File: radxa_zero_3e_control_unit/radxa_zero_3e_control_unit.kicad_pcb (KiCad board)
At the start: 2 copper layers, 186 x 65 mm, 122 parts, among them J1 USB STM32, J10 Valve, J11 ETH_IN, J12 ETH_OUT, J13 Compressor, J14 DebugUART, J15 Weight, J16 Malibotti, J17 Robot, J18 STLINK_V3_MINIE, J19 IO, J2 DC IN, J20 Bus-Servo, J21 STDC14, J22 USB STM32, J23 IO, J24 IO, J3 TOF3, J4 TOF2, J5 TOF1, J6 TOF1, J7 STEP1, J8 STEP2, J9 Conveyor, Q1 BC807, Q2 IRLML6344, Q3 IRLML6344, Q4 IRLML6344, U1 TPS54202DDC, U2 STM32G431RBTx, U3 HX711, U4 DCDC_MP2315, U5 TMC2209, U6 TMC2209, U7 PoE->24V, X1 Radxa Zero 3E

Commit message: Various
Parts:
- added J25: IO, Connector_JST:JST_XH_B6B-XH-A_1x06_P2.50mm_Vertical, F.Cu at (116.2, 95.7)
- added J26: IO, Connector_JST:JST_XH_B6B-XH-A_1x06_P2.50mm_Vertical, F.Cu at (156.6, 64.0)
- added J27: IO, Connector_JST:JST_XH_B6B-XH-A_1x06_P2.50mm_Vertical, F.Cu at (60.2, 93.4)
- C23: footprint Capacitor_THT:CP_Radial_D6.3mm_P2.50mm -> Capacitor_THT:CP_Radial_D8.0mm_P2.50mm
- moved FID2 8.33 mm to (152.7, 72.2)
- moved C23 0.90 mm to (150.1, 68.0)
- moved C33 0.50 mm to (122.2, 68.7)
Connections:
- J2 pad 1: GND -> 5-24V
- J2 pad 2: 5-24V -> GND
- J2 pad 3: unconnected-(J2-Pad3) -> GND
- U5 pad 9: GND -> +3V3
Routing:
- net +5V: track 96.6 -> 104.7 mm
- net +3V3: track 295.6 -> 302.3 mm, vias 9 -> 10
- net USBPD_D-: track 37.6 -> 42.5 mm
- net USBPD_D+: track 38.6 -> 42.9 mm
- net USB_VSENSE: track 49.4 -> 51.9 mm
- net 5-24V: track 177.1 -> 179.0 mm
- net GND: track 89.6 -> 91.6 mm, vias 347 -> 361
- net i2d: track 37.0 -> 37.7 mm
- net i2c: track 39.1 -> 39.8 mm
- net i1c: track 81.7 -> 82.4 mm
- net +9V: track 42.3 -> 43.0 mm
- net INT_TOF2: track 25.6 -> 26.3 mm
- net INT_TOF1: track 75.0 -> 75.7 mm
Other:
- board text added: "24V"
- board text added: "Stepper0"
- board text removed: "Stepper2"

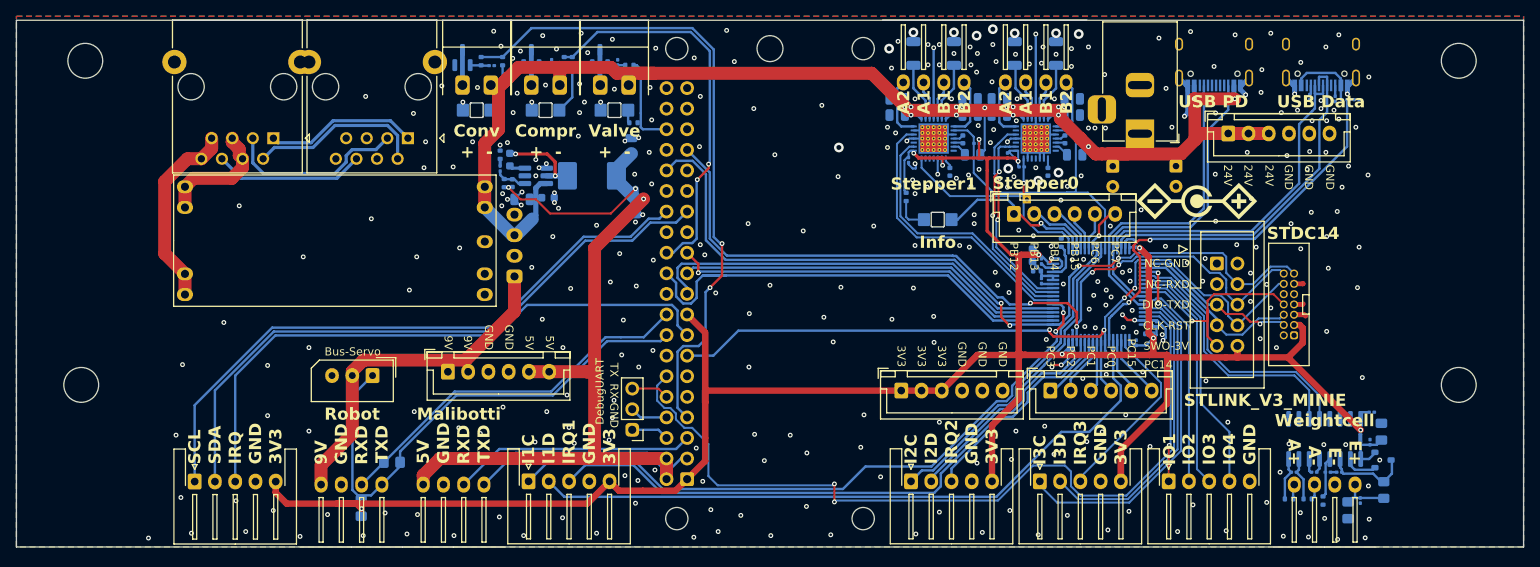
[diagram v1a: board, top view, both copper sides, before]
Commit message: Fixes
- air ventilation holes
- HX711 is on SPI MISO and SPI MOSI according to https://github.com/ufnalski/hx711_non_blocking_spi_g431kb (PC10-->PC11, PC11-->PC12)
- DC connector polarity changed
- connectors for voltages
- TMC2209 got different communication IDs
- Elkos mor space
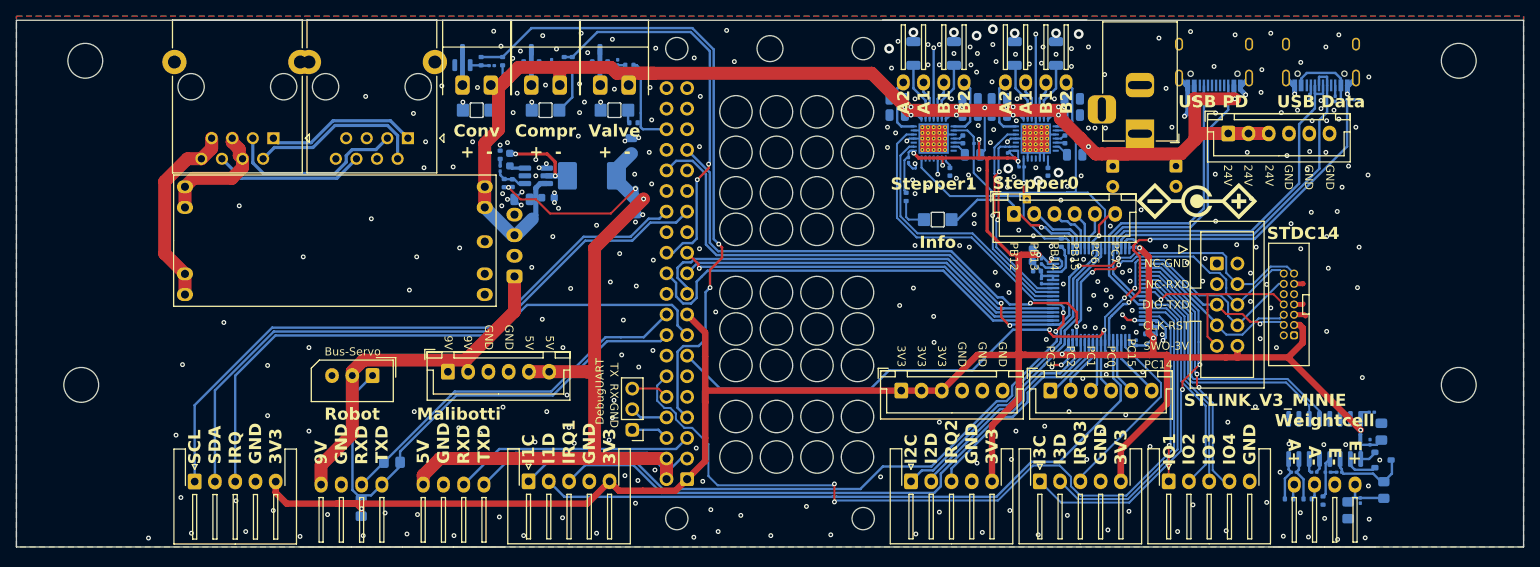
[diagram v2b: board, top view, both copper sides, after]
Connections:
- U2 pad 52: HX711_DATA -> IO4
- U2 pad 53: HX711_CLK -> HX711_DATA
- U2 pad 54: IO4 -> HX711_CLK
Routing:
- net STM32_RESET: track 91.2 -> 94.6 mm
- net SPI1_NSS: track 57.9 -> 55.6 mm
- net i3c: track 46.5 -> 48.1 mm
- net IO2: track 26.1 -> 27.6 mm
- net SWO: track 27.2 -> 26.2 mm
- net IO4: track 30.3 -> 31.1 mm, vias 0 -> 2
- net STEPPER_UART: track 31.5 -> 30.7 mm
- net HX711_DATA: track 33.1 -> 33.8 mm
- net HX711_CLK: track 32.0 -> 32.7 mm
- net IO3: track 28.7 -> 27.9 mm
- net SPI1_MISO: track 47.7 -> 48.2 mm
- net GND: vias 361 -> 340
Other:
- outline, holes or cut-outs redrawn

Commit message: WIP, before repinning SUM32G431
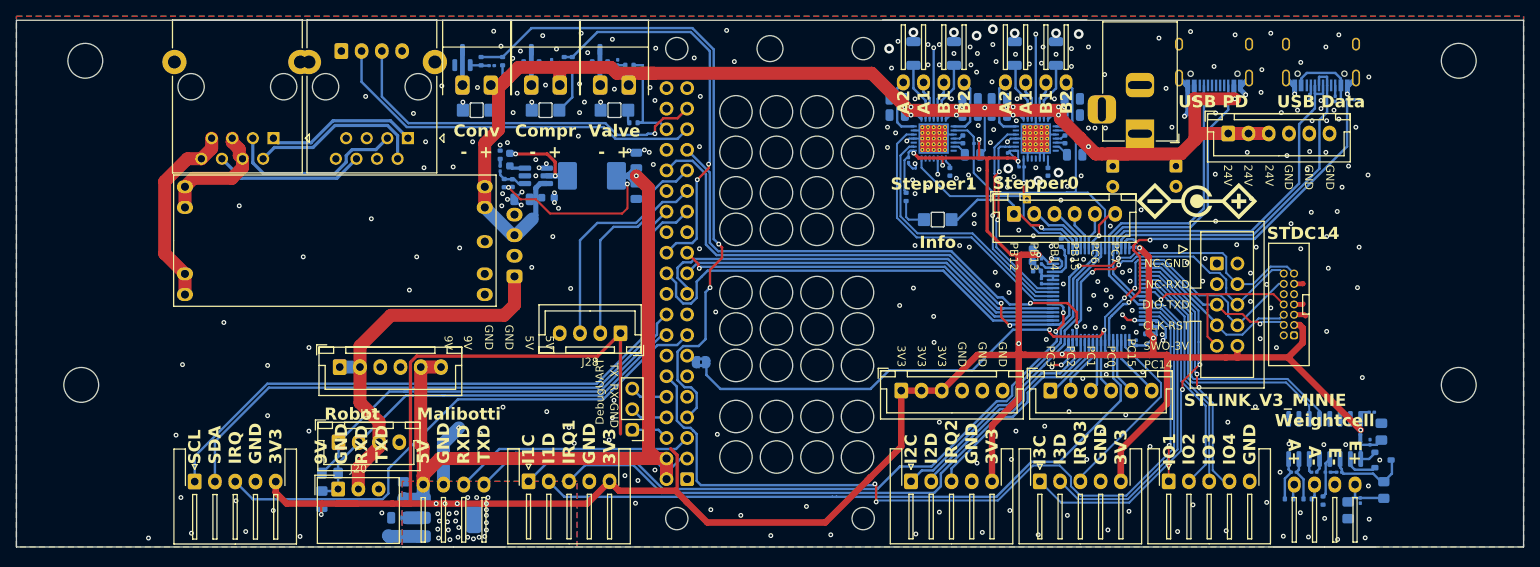
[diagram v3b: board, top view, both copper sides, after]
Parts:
- added C31: 10u, Capacitor_SMD:C_0805_2012Metric_Pad1.18x1.45mm_HandSolder, B.Cu at (54.8, 108.0)
- added C32: 22u, Capacitor_SMD:C_0805_2012Metric, B.Cu at (54.2, 111.4)
- added J28: RADXA I2C, Connector_JST:JST_XH_B4B-XH-A_1x04_P2.50mm_Vertical, F.Cu at (81.5, 88.6)
- added J29: RADXA GPIO, Connector_JST:JST_XH_B4B-XH-A_1x04_P2.50mm_Vertical, B.Cu at (47.1, 53.8)
- added JP1: STM_RST, Jumper:SolderJumper-2_P1.3mm_Bridged2Bar_RoundedPad1.0x1.5mm, B.Cu at (91.5, 92.2)
- added R33: 1k, Resistor_SMD:R_0402_1005Metric, B.Cu at (130.7, 88.9)
- added U8: AMS1117-3.3, Package_TO_SOT_SMD:SOT-223-3_TabPin2, B.Cu at (60.3, 111.4)
- J17: footprint liebler_CONN:JST_XH_S4B-XH-A-1_1x04_P2.50mm_Horizontal_SmallerCourtyard -> Connector_JST:JST_XH_B4B-XH-A_1x04_P2.50mm_Vertical
- J20: footprint Connector_Molex:Molex_SPOX_5267-03A_1x03_P2.50mm_Vertical -> Connector_Molex:Molex_SPOX_5268-03A_1x03_P2.50mm_Horizontal
- moved J20 14.6 mm to (46.7, 107.9), turned to 0 degrees
- moved J27 13.4 mm to (46.9, 92.8)
- moved R77 7.77 mm to (45.7, 105.9)
- moved J17 5.65 mm to (46.8, 102.1)
- moved R76 4.97 mm to (44.7, 109.1)
- moved C5 1.90 mm to (83.5, 71.1)
- moved C7 1.90 mm to (83.5, 67.3)
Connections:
- J17 pad 1: +9V -> ROBOT_RXD
- J17 pad 2: GND -> ROBOT_TXD
- J17 pad 3: ROBOT_RXD -> +9V
- J17 pad 4: ROBOT_TXD -> GND
- X1 pad 1: +3V3 -> unconnected-(X1-3V3-Pad1)
- X1 pad 13: STM32_RESET -> Net-(JP1-B)
- X1 pad 17: +3V3 -> unconnected-(X1-3V3-Pad17)
- X1 pad 29: unconnected-(X1-G3B3/-/-/I5C_SCL-Pad29) -> I5C_C
- X1 pad 31: unconnected-(X1-G3B4/-/-/I5C_SSDA-Pad31) -> I5C_D
- X1 pad 35: unconnected-(X1-G3A4/-/I3S_LRCK-Pad35) -> G3A4
- X1 pad 37: unconnected-(X1-G1A4/-/I1S_SCLK-Pad37) -> G1A4
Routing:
- net +3V3: track 302.3 -> 361.0 mm, vias 10 -> 38
- net G3A4: track 0.00 -> 47.4 mm
- net G1A4: track 0.00 -> 47.1 mm, vias 0 -> 1
- net I5C_D: track 0.00 -> 29.4 mm
- net I5C_C: track 0.00 -> 24.7 mm
- net +5V: track 104.7 -> 119.4 mm
- net GND: track 91.6 -> 103.6 mm, vias 340 -> 310
- net ROBOT_TXD: track 63.4 -> 52.6 mm
- net INT_RGB: track 75.1 -> 66.8 mm
- net ROBOT_RXD: track 46.3 -> 53.4 mm
- net +9V: track 43.0 -> 46.9 mm
- net SCL: track 77.6 -> 81.3 mm
- net SDA: track 78.7 -> 82.3 mm
- net STM32_RESET: track 94.6 -> 92.8 mm
- net Conveyor_PWM: track 81.0 -> 82.4 mm
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- added copper zone on B.Cu, net +3V3
- added copper zone on F.Cu, net +3V3
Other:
- board text added: "- +"
- board text removed: "+ -"

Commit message: Udated control unit pcb
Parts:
- removed J11: ETH_IN, liebler_CONN:RJ45_WithoutMagneticsTHT
- removed J17: Robot, Connector_JST:JST_XH_B4B-XH-A_1x04_P2.50mm_Vertical
- removed J18: STLINK_V3_MINIE, Connector_IDC:IDC-Header_2x05_P2.54mm_Vertical
- removed J19: IO, Connector_JST:JST_XH_S5B-XH-A-1_1x05_P2.50mm_Horizontal
- removed J23, J24, J25, J26, J27: IO, Connector_JST:JST_XH_B6B-XH-A_1x06_P2.50mm_Vertical
- removed J28: RADXA I2C, Connector_JST:JST_XH_B4B-XH-A_1x04_P2.50mm_Vertical
- removed J29: RADXA GPIO, Connector_JST:JST_XH_B4B-XH-A_1x04_P2.50mm_Vertical
- added C41: u1, Capacitor_SMD:C_0402_1005Metric, B.Cu at (48.2, 75.5)
- added H3: M2,5, MountingHole:MountingHole_2.7mm, F.Cu at (137.5, 53.5)
- added H4: M2,5, MountingHole:MountingHole_2.7mm, F.Cu at (137.5, 111.5)
- added J30: LightBarrier1, liebler_CONN:JST_XH_B3B-XH-A_1x03_P2.50mm_Vertical_smaller, F.Cu at (67.1, 66.4)
- added J31: LightBarrier2, liebler_CONN:JST_XH_B3B-XH-A_1x03_P2.50mm_Vertical_smaller, F.Cu at (67.1, 60.2)
- added J32: LightBarrier3, liebler_CONN:JST_XH_B3B-XH-A_1x03_P2.50mm_Vertical_smaller, F.Cu at (56.8, 60.2)
- added J33: PressureTransducer, liebler_CONN:JST_XH_B3B-XH-A_1x03_P2.50mm_Vertical_smaller, F.Cu at (79.8, 53.8)
- added JP2: 5-24, Jumper:SolderJumper-3_P1.3mm_Open_RoundedPad1.0x1.5mm_NumberLabels, B.Cu at (67.1, 64.6)
- added JP3: 5-24, Jumper:SolderJumper-3_P1.3mm_Open_RoundedPad1.0x1.5mm_NumberLabels, B.Cu at (67.1, 58.4)
- added JP4: 5-24, Jumper:SolderJumper-3_P1.3mm_Open_RoundedPad1.0x1.5mm_NumberLabels, B.Cu at (56.8, 58.4)
- added M1: W5500_mini, liebler_MODULES:W5500-mini, F.Cu at (98.2, 82.5)
- added M2: FanMech, liebler_MECH:FAN2507, F.Cu at (113.0, 82.5)
- added M3: FanElek, Connector_JST:JST_XH_B2B-XH-A_1x02_P2.50mm_Vertical, F.Cu at (79.8, 66.4)
- added R32: 10k, Resistor_SMD:R_0402_1005Metric, B.Cu at (83.4, 56.0)
- added R34: 10k, Resistor_SMD:R_0402_1005Metric, B.Cu at (82.9, 63.4)
- added R35: 10k, Resistor_SMD:R_0402_1005Metric, B.Cu at (53.4, 71.8)
- added R36: 1k, Resistor_SMD:R_0402_1005Metric, B.Cu at (50.0, 79.2)
- added X2: MT3608, liebler_MODULES:DCDC_MT3608, B.Cu at (136.2, 82.8)
- C11, C12, C13, C15, C16, C17, C18, C19, C20, C21, C27, C28, C6, C9: footprint Capacitor_SMD:C_0201_0603Metric -> Capacitor_SMD:C_0402_1005Metric
- C24: footprint Capacitor_THT:CP_Radial_D6.3mm_P2.50mm -> Capacitor_THT:CP_Radial_D8.0mm_P2.50mm
- C31: footprint Capacitor_SMD:C_0805_2012Metric_Pad1.18x1.45mm_HandSolder -> Capacitor_SMD:C_0805_2012Metric
- H6: footprint MountingHole:MountingHole_3.2mm_M3 -> MountingHole:MountingHole_2.7mm
- J12: value ETH_OUT -> CAN; footprint liebler_CONN:RJ45_WithoutMagneticsTHT -> liebler_CONN:JST_XH_B3B-XH-A_1x03_P2.50mm_Vertical_smaller
- J15, J16, J7, J8: footprint liebler_CONN:JST_XH_S4B-XH-A-1_1x04_P2.50mm_Horizontal_SmallerCourtyard -> liebler_CONN:JST_XH_B4B-XH-A_1x04_P2.50mm_Vertical_smaller
- J20: footprint Connector_Molex:Molex_SPOX_5268-03A_1x03_P2.50mm_Horizontal -> Connector_Molex:Molex_SPOX_5267-03A_1x03_P2.50mm_Vertical
- J3, J4, J5: footprint Connector_JST:JST_XH_S5B-XH-A-1_1x05_P2.50mm_Horizontal -> liebler_CONN:JST_XH_B5B-XH-A_1x05_P2.50mm_Vertical_smaller
- J6: value TOF1 -> RGB; footprint Connector_JST:JST_XH_S5B-XH-A-1_1x05_P2.50mm_Horizontal -> liebler_CONN:JST_XH_B5B-XH-A_1x05_P2.50mm_Vertical_smaller
- R10, R11, R21, R24, R27, R3, R8, R9: footprint Resistor_SMD:R_0201_0603Metric -> Resistor_SMD:R_0402_1005Metric
- R76, R77: footprint Resistor_SMD:R_0805_2012Metric_Pad1.20x1.40mm_HandSolder -> Resistor_SMD:R_0402_1005Metric
- TP1: footprint TestPoint:TestPoint_THTPad_1.0x1.0mm_Drill0.5mm -> TestPoint:TestPoint_THTPad_D1.0mm_Drill0.5mm
- U4: moved to B.Cu
- U7: value PoE->24V -> SIT3051TK; footprint liebler_MODULES:XC7010_DCDC_ISOLATED_MODUEL -> Package_DFN_QFN:DFN-8-1EP_3x3mm_P0.65mm_EP1.55x2.4mm; moved to B.Cu
- moved L2 159.1 mm to (26.0, 54.2), turned to -90 degrees
- moved Q1 157.9 mm to (24.7, 57.9), turned to 90 degrees
- moved C22 155.0 mm to (25.3, 62.4), turned to -90 degrees
- moved C20 154.6 mm to (25.3, 60.0), turned to 0 degrees
- moved C10 154.1 mm to (28.9, 51.8), turned to 180 degrees
- moved C6 152.5 mm to (31.8, 51.3), turned to 0 degrees
- moved R30 152.3 mm to (27.1, 105.6), turned to 90 degrees
- moved NT1 150.4 mm to (27.2, 63.9), turned to 180 degrees
- moved R29 150.2 mm to (27.9, 105.6), turned to -90 degrees
- moved R8 149.6 mm to (29.3, 55.6), turned to 0 degrees
- moved C21 149.4 mm to (28.9, 64.0)
- moved J22 149.0 mm to (30.4, 111.1), turned to 180 degrees
- moved R28 148.4 mm to (28.6, 105.6), turned to 90 degrees
- moved R7 147.9 mm to (31.8, 52.3), turned to 180 degrees
- moved R11 146.5 mm to (31.2, 55.6), turned to 0 degrees
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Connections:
- net PB12 renamed ADC1_IN11
- net i1c renamed I2C2_SCL
- net i1d renamed I2C2_SDA
- J10 pad 1: 5-24V -> +24V
- J12 pad 1: Net-(J11-Pad1) -> CANH
- J12 pad 2: Net-(J11-Pad2) -> GND
- J12 pad 3: Net-(J11-Pad3) -> CANL
- J13 pad 1: 5-24V -> +24V
- J16 pad 1: +5V -> MALIBOTTI_U1R
- J16 pad 2: GND -> MALIBOTTI_U1T
- J16 pad 3: MALIBOTTI_RXD -> GND
- J16 pad 4: MALIBOTTI_TXD -> +5V
- J20 pad 1: ROBOT_TXD -> ROBOT_U4R
- J3 pad 1: i3c -> I2C3_SCL
- J3 pad 2: i3d -> I2C3_SDA
- J4 pad 3: INT_TOF1 -> INT_TOF2
- J5 pad 1: i2c -> I2C1_SCL
- J5 pad 2: i2d -> I2C1_SDA
- J5 pad 3: INT_TOF2 -> INT_TOF1
- J6 pad 1: SCL -> I2C1_SCL
- J6 pad 2: SDA -> I2C1_SDA
- J9 pad 1: 5-24V -> +24V
- R19 pad 2: Conveyor_PWM -> CONVEYOR_T2C2
- R20 pad 2: Conveyor_PWM -> CONVEYOR_T2C2
- R22 pad 2: Valve -> VALVE
- R23 pad 2: Valve -> VALVE
- R25 pad 2: Compressor_PWM -> COMPRESSOR_T2C1
- R26 pad 2: Compressor_PWM -> COMPRESSOR_T2C1
- R76 pad 2: ROBOT_TXD -> ROBOT_U4R
- R77 pad 1: ROBOT_RXD -> ROBOT_U4T
- R77 pad 2: ROBOT_TXD -> ROBOT_U4R
- U2 pad 10: T1C3 -> PRESSURE_ADC
- U2 pad 11: T1C4 -> W5500_IRQ
- U2 pad 12: INT_TOF2 -> COMPRESSOR_T2C1
- U2 pad 13: INT_TOF1 -> CONVEYOR_T2C2
- U2 pad 2: INT_TOF3 -> LightBarrier3
- U2 pad 23: Stepper1_Dir -> VALVE
- U2 pad 24: Stepper1_Step -> STEPPER1_DIR
- U2 pad 25: Stepper2_Step -> STEPPER1_STEP
- U2 pad 26: Stepper2_Dir -> ADC2_12
- U2 pad 3: PC14 -> LightBarrier2
- U2 pad 35: PB13 -> STEPPER_EN
- U2 pad 36: T15C1 -> HX711_SPI2_MISO
- U2 pad 37: T15C2 -> HX711_SPI2_MOSI
- U2 pad 38: T8C1 -> STEPPER2_DIR_T3C1_T8C1
- U2 pad 39: T8C2 -> STEPPER2_STEP_T3C2_T8C2
- U2 pad 4: PC15 -> INT_TOF3
- U2 pad 40: i2c -> I2C3_SCL
- U2 pad 41: i2d -> I2C3_SDA
- U2 pad 42: STEPPER_EN -> USB_VSENSE
- U2 pad 51: i3c -> I2C1_SCL
- U2 pad 52: IO4 -> ROBOT_U4T
- U2 pad 53: HX711_DATA -> ROBOT_U4R
- U2 pad 54: HX711_CLK -> INT_TOF1
- U2 pad 55: IO3 -> INT_RGB
- U2 pad 58: IO2 -> INT_TOF2
- U2 pad 6: USB_VSENSE -> LightBarrier1
- U2 pad 60: i3d -> I2C1_SDA
- U2 pad 61: STM32_BOOT -> STM32_BOOT_CAN_RX
- U2 pad 62: IO1 -> CAN_TX
- U2 pad 8: T1C1-LU1R -> MALIBOTTI_U1R
- U2 pad 9: T1C2-LU1T -> MALIBOTTI_U1T
- U3 pad 11: HX711_CLK -> HX711_SPI2_MOSI
- U3 pad 12: HX711_DATA -> HX711_SPI2_MISO
- U5 pad 10: GND -> +3V3
- U5 pad 16: Stepper1_Step -> STEPPER1_STEP
- U5 pad 19: Stepper1_Dir -> STEPPER1_DIR
- U5 pad 9: +3V3 -> GND
- U6 pad 16: Stepper2_Step -> STEPPER2_STEP_T3C2_T8C2
- U6 pad 19: Stepper2_Dir -> STEPPER2_DIR_T3C1_T8C1
- U7 pad 1: +48V -> Net-(U7-D)
- U7 pad 2: +48V -> GND
- U7 pad 3: GND1 -> +3V3
- U7 pad 4: GND1 -> CAN_TX
- U7 pad 5: GND -> unconnected-(U7-SHDN(PD)-Pad5)
- U7 pad 6: GND -> CANL
- U7 pad 7: unconnected-(U7-VADJ-Pad7) -> CANH
- U7 pad 8: 5-24V -> Net-(U7-Rs)
- U7 pad 9: 5-24V -> GND
- X1 pad 12: STM32_BOOT -> unconnected-(X1-G3A3-Pad12)
- X1 pad 13: Net-(JP1-B) -> unconnected-(X1-G3A2/-/-/I2S3_MCLK-Pad13)
- X1 pad 15: INT_RGB -> unconnected-(X1-G3B0-Pad15)
- X1 pad 16: ROBOT_TXD -> unconnected-(X1-G3B1/U4R/PWM8-Pad16)
- X1 pad 18: ROBOT_RXD -> unconnected-(X1-G3B2/U4T/PWM9-Pad18)
- X1 pad 24: Compressor_PWM -> unconnected-(X1-G4C6/S3_CS0/PWM13/U9R/I3S_SDI-Pad24)
- X1 pad 29: I5C_C -> unconnected-(X1-G3B3/-/-/I5C_SCL-Pad29)
- X1 pad 3: MALIBOTTI_TXD -> unconnected-(X1-G1A0/U3R/PU!-Pad3)
- X1 pad 31: I5C_D -> unconnected-(X1-G3B4/-/-/I5C_SSDA-Pad31)
- X1 pad 35: G3A4 -> unconnected-(X1-G3A4/-/I3S_LRCK-Pad35)
- X1 pad 36: Valve -> Net-(JP1-B)
- X1 pad 37: G1A4 -> unconnected-(X1-G1A4/-/I1S_SCLK-Pad37)
- X1 pad 38: unconnected-(X1-G3A6/-/-/-/I3S_SDI-Pad38) -> STM32_BOOT_CAN_RX
- X1 pad 5: MALIBOTTI_RXD -> unconnected-(X1-G1A1/U3T/PU!-Pad5)
- X1 pad 7: Conveyor_PWM -> unconnected-(X1-G3C4/-/-/PWM14_M0-Pad7)
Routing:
- net +3V3: track 361.0 -> 181.9 mm, vias 38 -> 110
- net +24V: track 0.00 -> 176.3 mm, vias 0 -> 3
- net STM32_BOOT: track 102.1 -> 0.00 mm, vias 2 -> 0
- net GND: track 103.6 -> 201.8 mm, vias 310 -> 224
- net Conveyor_PWM: track 82.4 -> 0.00 mm, vias 2 -> 0
- net SDA: track 82.3 -> 0.00 mm
- net SCL: track 81.3 -> 0.00 mm
- net VALVE: track 0.00 -> 80.6 mm
- net COMPRESSOR_T2C1: track 0.00 -> 75.3 mm, vias 0 -> 2
- net I2C3_SDA: track 0.00 -> 69.4 mm
- net I2C3_SCL: track 0.00 -> 66.8 mm
- net CONVEYOR_T2C2: track 0.00 -> 62.0 mm, vias 0 -> 2
- net I2C2_SDA: track 84.1 -> 25.8 mm, vias 0 -> 2
- net HX711_SPI2_MISO: track 0.00 -> 53.6 mm, vias 0 -> 2
- net ROBOT_RXD: track 53.4 -> 0.00 mm
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- added copper zone on B.Cu, net 5-24V
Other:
- outline, holes or cut-outs redrawn
- board text added: "FAN"
- board text added: "I2C1"
- board text added: "I2C2"
- board text added: "I2C3"
- board text added: "L CAN H"
- board text added: "LB1"
- board text added: "LB2"
- board text added: "LB3"
- board text added: "Pressure"
- board text added: "Stepper2"
- board text removed: "24V"
- board text removed: "5V"
- board text removed: "9V"
- board text removed: "CLK-RST"
- board text removed: "DIO-TXD"
- board text removed: "I1C"
- board text removed: "I1D"
- board text removed: "I2C"
- board text removed: "I2D"
- board text removed: "I3C"
- board text removed: "I3D"
- board text removed: "IO1"
- board text removed: "IO2"
- board text removed: "IO3"
- board text removed: "IO4"
- board text removed: "IRQ1"
- board text removed: "IRQ2"
- board text removed: "IRQ3"
- board text removed: "NC-GND"
- board text removed: "NC-RXD"
- board text removed: "PB12"
- board text removed: "PB13"
- board text removed: "PB14"
- board text removed: "PB15"
- board text removed: "PC0"
- board text removed: "PC1"
- board text removed: "PC14"
- board text removed: "PC15"
- board text removed: "PC2"
- board text removed: "PC3"
- board text removed: "PC6"
- board text removed: "PC7"
- board text removed: "RXD"
- board text removed: "SWO-3V"
- board text removed: "Stepper0"
- board text removed: "TXD"

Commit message: Sigmoid Stepper
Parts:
- added C44: u1, Capacitor_SMD:C_0402_1005Metric, B.Cu at (46.5, 101.9)
- added R37: R, Resistor_SMD:R_2010_5025Metric, B.Cu at (48.9, 103.1)
- added R38: 5k1, Resistor_SMD:R_0201_0603Metric, B.Cu at (47.1, 99.5)
- added R39: 5k1, Resistor_SMD:R_0201_0603Metric, B.Cu at (47.1, 98.7)
- added R40: 5k1, Resistor_SMD:R_0201_0603Metric, B.Cu at (54.4, 72.8)
- added R41: 5k1, Resistor_SMD:R_0201_0603Metric, B.Cu at (66.7, 80.0)
- added R42: 5k1, Resistor_SMD:R_0201_0603Metric, B.Cu at (47.1, 72.8)
- added R43: 5k1, Resistor_SMD:R_0201_0603Metric, B.Cu at (48.5, 83.8)
- added U9: INA226, Package_SO:VSSOP-10_3x3mm_P0.5mm, B.Cu at (44.5, 99.2)
- moved C24 0.85 mm to (50.3, 96.0)
- moved C23 0.85 mm to (58.8, 96.0)
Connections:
- J1 pad A4: 5-24V -> +VDC
- J1 pad A9: 5-24V -> +VDC
- J1 pad B4: 5-24V -> +VDC
- J1 pad B9: 5-24V -> +VDC
- J2 pad 1: 5-24V -> +VDC
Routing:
- net +VDC: track 0.00 -> 36.0 mm, vias 0 -> 2
- net +3V3: track 181.9 -> 216.1 mm, vias 110 -> 113
- net I2C3_SDA: track 69.4 -> 92.7 mm
- net I2C3_SCL: track 66.8 -> 89.2 mm
- net GND: track 201.8 -> 190.8 mm, vias 224 -> 221
- net 5-24V: track 191.0 -> 180.9 mm, vias 24 -> 22
- net I2C2_SCL: track 36.2 -> 39.4 mm
- net SPI1_MOSI: track 51.1 -> 50.0 mm
- net LightBarrier1: track 18.2 -> 17.5 mm
- net Net-(Q2-G): track 3.86 -> 3.11 mm
- net USBPD_CC1: track 42.2 -> 42.9 mm
- net STM32BOOT_TXD: track 63.3 -> 62.5 mm
- net W5500_IRQ: track 42.0 -> 41.3 mm
- net MALIBOTTI_U1T: track 29.5 -> 28.8 mm
- net MALIBOTTI_U1R: track 28.7 -> 28.0 mm
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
